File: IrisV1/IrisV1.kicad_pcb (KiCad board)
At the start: 2 copper layers, 36.7 x 75 mm, 93 parts, among them J1 Conn_02x02_Odd_Even, J13 TB002-500-02BE, J14 TB002-500-02BE, J16 TB002-500-02BE, J21 TB002-500-02BE, J22 TB002-500-02BE, J3 USB4110GFA, J4 Conn_01x04, J5 MSD-10-C, J6 MSD-10-C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

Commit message: Iris final update to inbuilt library
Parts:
- A3: footprint Baro 1:XDCR_LPS22DFTR -> UNSW Rocketry Library:XDCR_LPS22DFTR
- J13, J14, J16, J21, J22: footprint screw terminal:CUI_TB002-500-02BE -> UNSW Rocketry Library:CUI_TB002-500-02BE
- J3: footprint USB:GCT_USB4110GFA -> UNSW Rocketry Library:GCT_USB4110GFA
- J5, J6: footprint microSd card locking:CUI_MSD-10-C -> UNSW Rocketry Library:CUI_MSD-10-C
- L1: footprint inductor:1277AS-H-1R0M=P2_MUR-M -> UNSW Rocketry Library:1277AS-H-1R0M=P2_MUR-M
- LS1: footprint low volt buzzer:SPKR_CMI-1295-03TH -> UNSW Rocketry Library:SPKR_CMI-1295-03TH
- Q1: footprint pyro 1:SOIC_09DY-T1-GE3_VIS -> UNSW Rocketry Library:SOIC_09DY-T1-GE3_VIS
- Q2: footprint npn 1:SOT-363&slash_SC-88&slash_SC70-6&slash_CASE419B_OSI -> UNSW Rocketry Library:SOT-363&slash_SC-88&slash_SC70-6&slash_CASE419B_OSI
- R3, R4, R5, R6: value 1.3k -> 100
- U1: footprint Acc 1:QFN_LSM6DSV80XTR_STM -> UNSW Rocketry Library:QFN_LSM6DSV80XTR_STM
- U18: footprint ms5611:SON8_MS5611_TEC -> UNSW Rocketry Library:SON8_MS5611_TEC
- U2: footprint esd:DBV0005A_L -> UNSW Rocketry Library:DBV0005A_N
- U20: footprint BMI323:BMI323_BOS -> UNSW Rocketry Library:BMI323_BOS
- U22: footprint TPS63070:RNM0015A -> UNSW Rocketry Library:RNM0015A
- U3: footprint ESP32-S3:XCVR_ESP32-S3-WROOM-1U-N4 -> UNSW Rocketry Library:XCVR_ESP32-S3-WROOM-1U-N4
- moved U2 0.11 mm to (143.6, 72.8)

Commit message: Centralised Library
Updating to a centralised library structure
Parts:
- G***: footprint Logos:RocketryLogo -> UNSW Rocketry Library:RocketryLogo

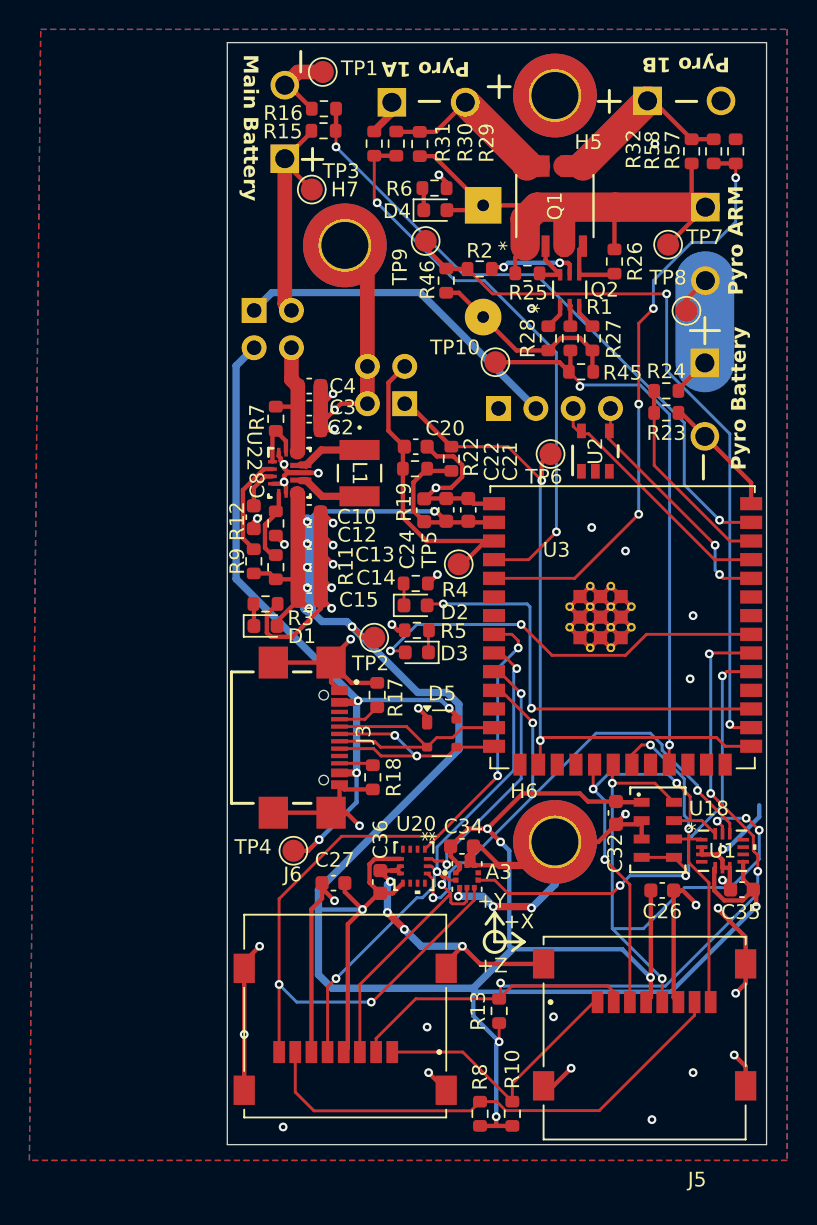
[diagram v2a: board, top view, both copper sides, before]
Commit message: Changed to 3.5mm Screw terminals
All screw terminals in IRIS changed to 3.5mm screw terminals per Oliver's request.
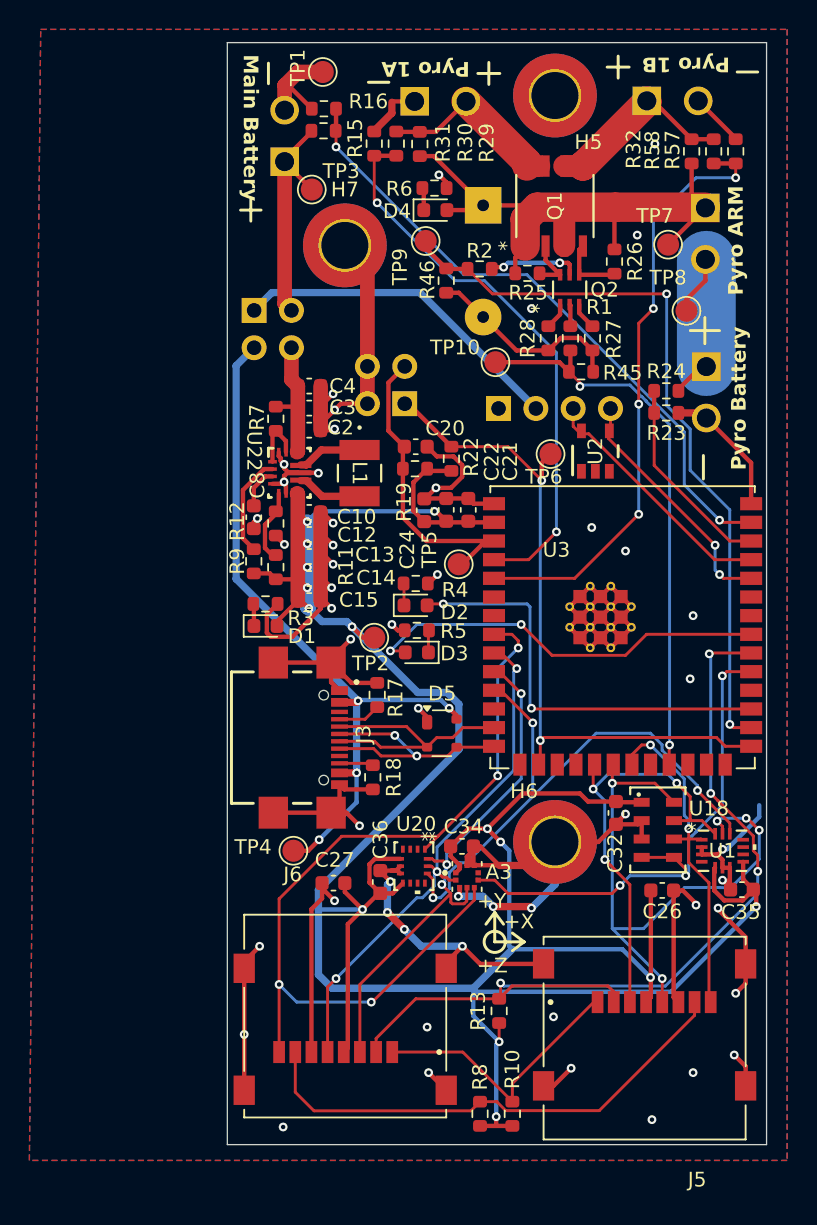
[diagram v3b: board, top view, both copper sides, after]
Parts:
- J13, J14, J16, J21, J22: footprint UNSW Rocketry Library:CUI_TB002-500-02BE -> UNSW Rocketry Library:ADAMTECH_EBWA-02-A
- moved J22 3.30 mm to (133.0, 49.0)
- moved J16 2.00 mm to (151.1, 68.8)
- moved J14 1.80 mm to (151.0, 58.0)
- moved J21 1.70 mm to (148.8, 49.0)
- moved J13 1.55 mm to (122.4, 51.4)
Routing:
- net GND: track 256.8 -> 264.5 mm, vias 50 -> 51
- net Battery2: track 10.8 -> 13.9 mm
- net Pyro 1B cont: track 40.7 -> 41.3 mm
